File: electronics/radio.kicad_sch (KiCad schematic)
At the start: 26 parts, among them J7 SIM_Card, J9 Conn_Coaxial_Small, U2 TPS22953

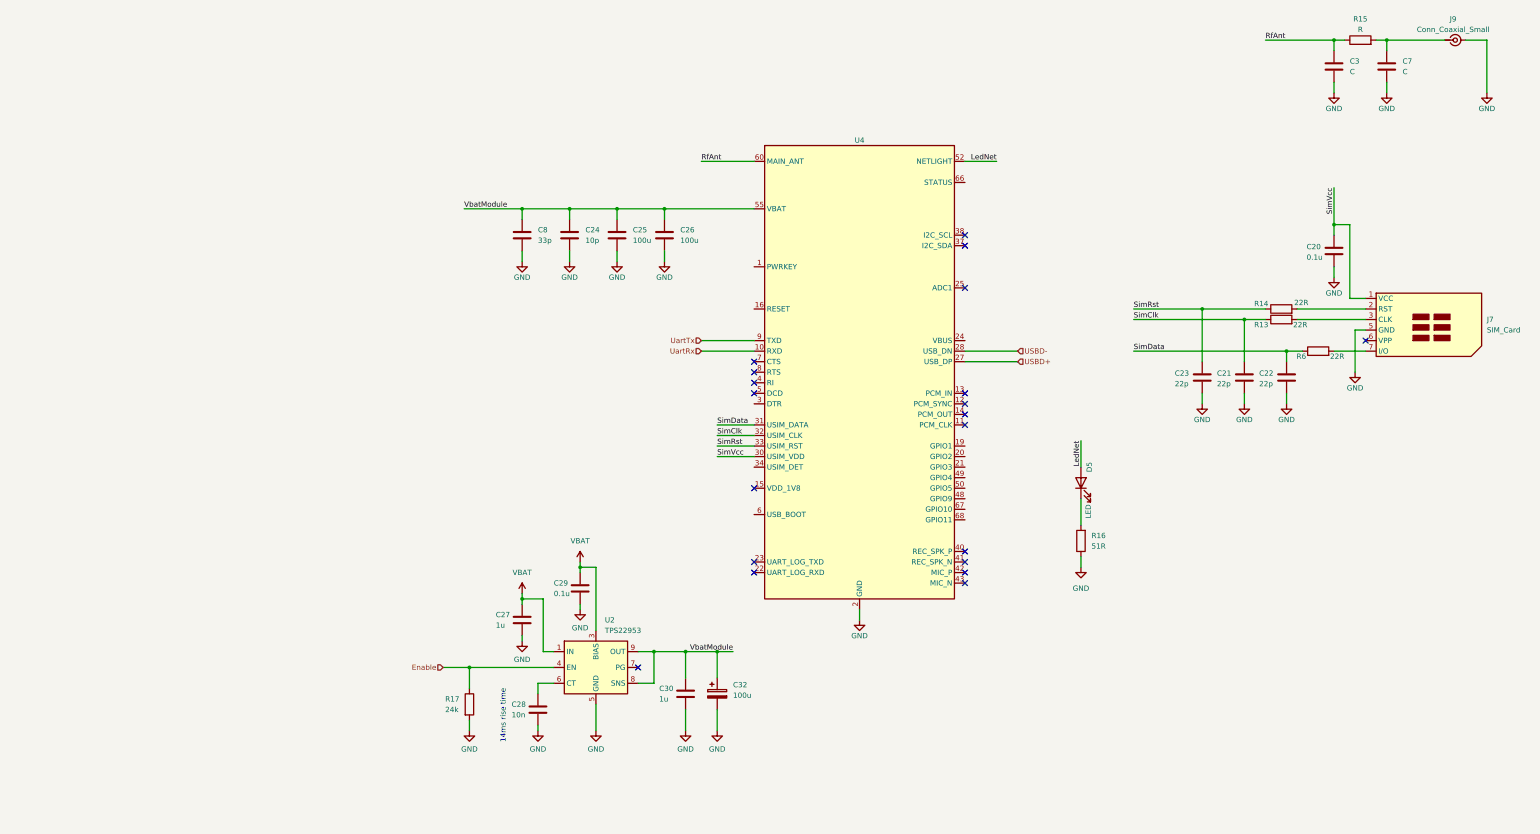
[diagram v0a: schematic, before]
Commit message: electronics: replace charger
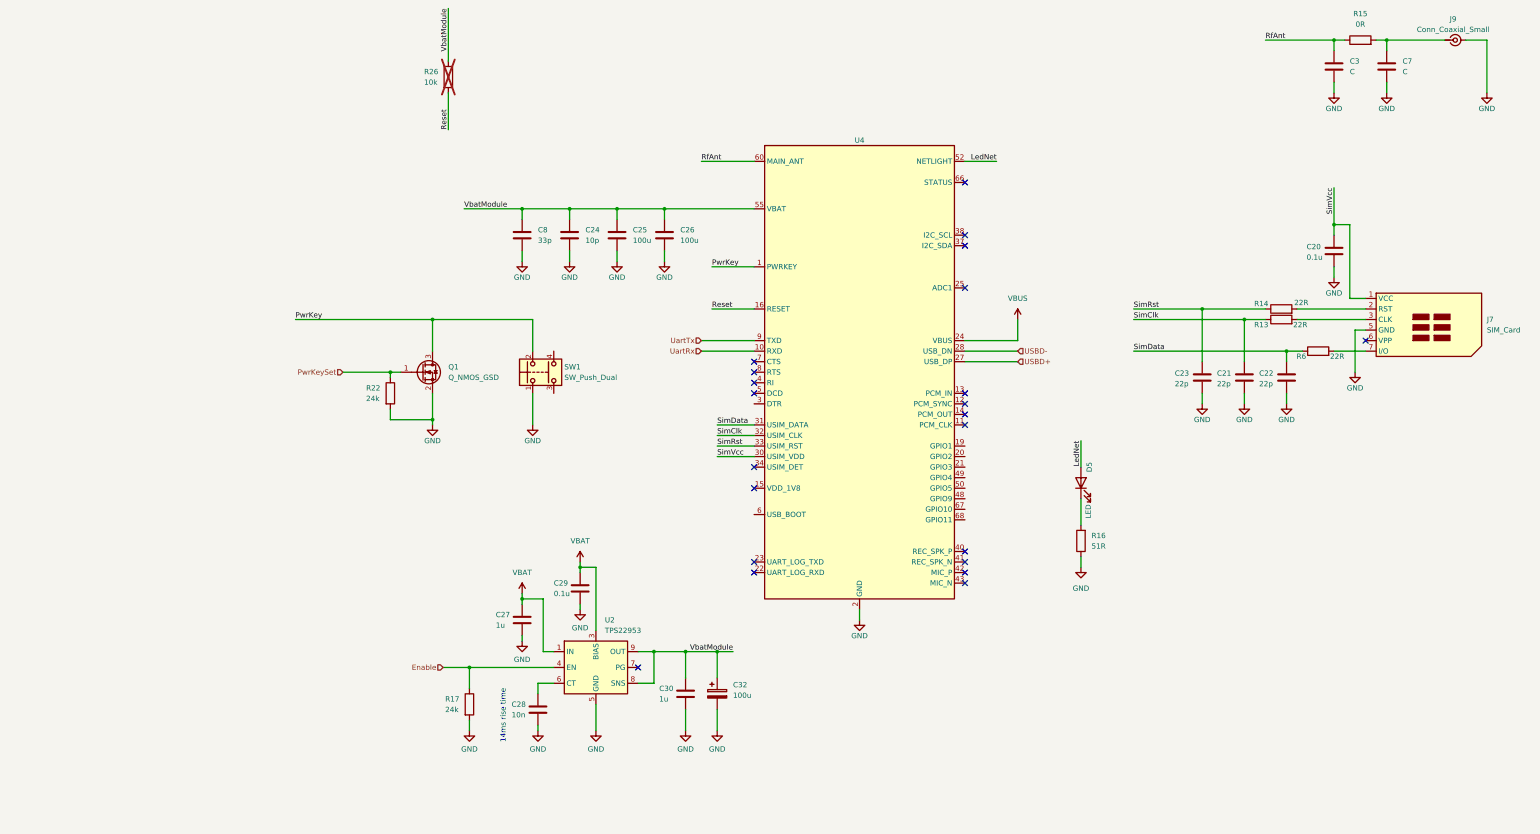
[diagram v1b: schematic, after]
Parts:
- added Q1: Q_NMOS_GSD, symbol Transistor_FET:Q_NMOS_GSD
- added R22: 24k, Resistor_SMD:R_0402_1005Metric, symbol Device:R
- added R26: 10k, Resistor_SMD:R_0402_1005Metric, symbol Device:R
- added SW1: SW_Push_Dual, symbol Switch:SW_Push_Dual
- C20, C21, C22, C23, C24, C8: footprint (none) -> Capacitor_SMD:C_0603_1608Metric
- C25, C26: footprint (none) -> Capacitor_SMD:C_1210_3225Metric
- C3, C7: footprint (none) -> Capacitor_SMD:C_0402_1005Metric
- C32: footprint portsupply:CP_Elec_6.3x7.7 -> Capacitor_SMD:CP_Elec_6.3x7.7
- J7: footprint (none) -> Connector_Card:nanoSIM_Hinged_CUI_NSIM-2-C
- R13, R14, R6: footprint (none) -> Resistor_SMD:R_0603_1608Metric
- R15: value R -> 0R; footprint (none) -> Resistor_SMD:R_0402_1005Metric
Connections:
- net GND: now also Q1.2 (S), R22.2, SW1.1
- net VBAT: now also R26.1
- net PwrKey: now reaches U4.1 (PWRKEY)
- net PwrKey: now also Q1.3 (D), SW1.2
- net Reset: now reaches U4.16 (RESET)
- net Reset: now also R26.2
- net VBUS: now reaches U4.24 (VBUS)
- new net PwrKeySet: Q1.1 (G), R22.1
- no-connect marks 20 -> 22

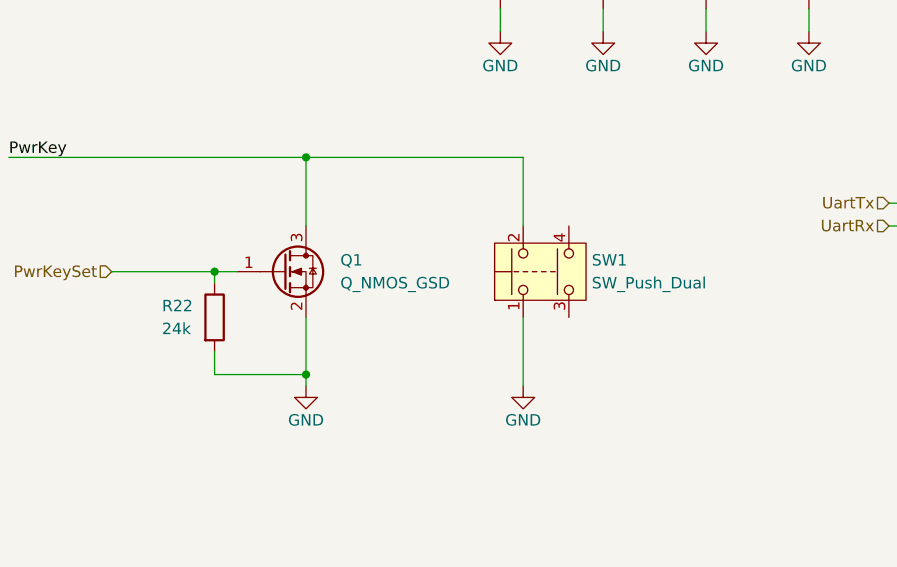
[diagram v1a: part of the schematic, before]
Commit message: electronics: select footprints
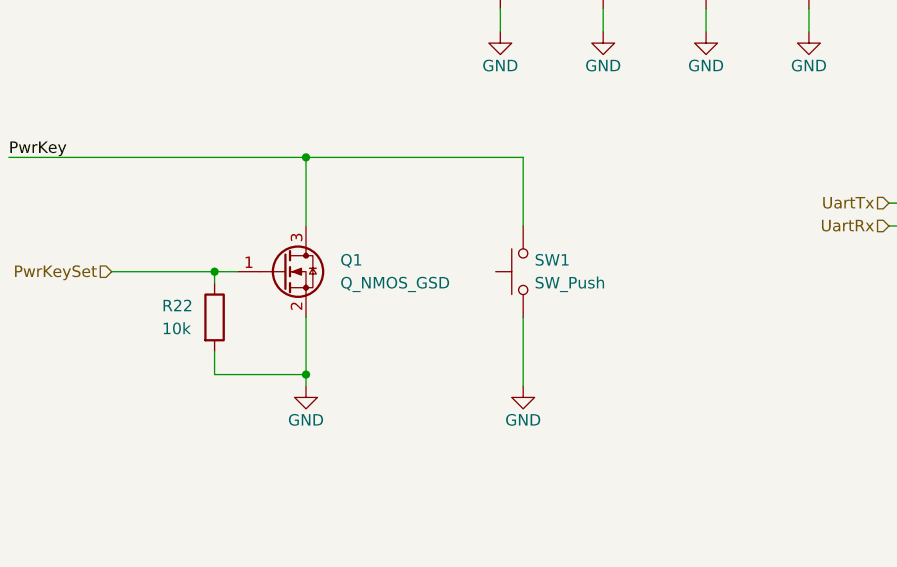
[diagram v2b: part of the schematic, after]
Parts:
- removed SW1: SW_Push_Dual, symbol Switch:SW_Push_Dual
- added SW1: SW_Push, Button_Switch_SMD:SW_SPST_TL3305A, symbol Switch:SW_Push
- J9: footprint (none) -> Connector_Coaxial:U.FL_Hirose_U.FL-R-SMT-1_Vertical; MPN (none) -> U.FL-R-SMT-1(01)
- R22: value 24k -> 10k
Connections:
- net GND: now also SW1.1
- net PwrKey: now also SW1.2
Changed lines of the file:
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@@
 	)
 	(symbol
-		(lib_id "Switch:SW_Push_Dual")
-		(at 48.26 101.6 90)
-		(unit 1)
-		(body_style 1)
-		(exclude_from_sim no)
-		(in_bom yes)
-		(on_board yes)
-		(in_pos_files yes)
-		(dnp no)
-		(fields_autoplaced yes)
-		(property "Reference" "SW1"
-			(at 53.34 100.3299 90)
-			(show_name no)
-			(do_not_autoplace no)
-			(effects
-				(font
-					(size 1.27 1.27)
-				)
-				(justify right)
-			)
-		)
-		(property "Value" "SW_Push_Dual"
-			(at 53.34 102.8699 90)
-			(show_name no)
-			(do_not_autoplace no)
-			(effects
-				(font
-					(size 1.27 1.27)
-				)
-				(justify right)
-			)
-		)
-		(property "Footprint" ""
-			(at 40.64 101.6 0)
-			(hide yes)
-			(show_name no)
-			(do_not_autoplace no)
-			(effects
-				(font
-					(size 1.27 1.27)
-				)
-			)
-		)
-		(property "Datasheet" ""
-			(at 48.26 101.6 0)
-			(hide yes)
-			(show_name no)
-			(do_not_autoplace no)
-			(effects
-				(font
-					(size 1.27 1.27)
-				)
-			)
-		)
-		(property "Description" "Push button switch, generic, symbol, four pins"
-			(at 48.26 101.6 0)
-			(hide yes)
-			(show_name no)
-			(do_not_autoplace no)
-			(effects
-				(font
-					(size 1.27 1.27)
-				)
-			)
-		)
-		(pin "1"
-		)
-		(pin "2"
-		)
-		(pin "4"
-		)
-		(pin "3"
-		)
-		(instances
-			(project "MyScale"
-				(path "/b5eed584-7820-40e8-871b-2aa5dd8c83ec/d79f2b7f-8f6c-4118-9551-ed509f2ef890"
-					(reference "SW1")
-					(unit 1)
-				)
-			)
-		)
-	)
-	(symbol
 		(lib_id "power:GND")
 		(at 43.18 166.37 0)
@@
 			)
 		)
-		(property "Value" "24k"
+		(property "Value" "10k"
 			(at 5.588 107.95 0)
 			(show_name no)
@@
 	)
 	(symbol
+		(lib_id "Switch:SW_Push")
+		(at 45.72 101.6 90)
+		(unit 1)
+		(body_style 1)
+		(exclude_from_sim no)
+		(in_bom yes)
+		(on_board yes)
+		(in_pos_files yes)
+		(dnp no)
+		(fields_autoplaced yes)
+		(property "Reference" "SW1"
+			(at 46.99 100.3299 90)
+			(show_name no)
+			(do_not_autoplace no)
+			(effects
+				(font
+					(size 1.27 1.27)
+				)
+				(justify right)
+			)
+		)
+		(property "Value" "SW_Push"
+			(at 46.99 102.8699 90)
+			(show_name no)
+			(do_not_autoplace no)
+			(effects
+				(font
+					(size 1.27 1.27)
+				)
+				(justify right)
+			)
+		)
+		(property "Footprint" "Button_Switch_SMD:SW_SPST_TL3305A"
+			(at 40.64 101.6 0)
+			(hide yes)
+			(show_name no)
+			(do_not_autoplace no)
+			(effects
+				(font
+					(size 1.27 1.27)
+				)
+			)
+		)
+		(property "Datasheet" ""
+			(at 40.64 101.6 0)
+			(hide yes)
+			(show_name no)
+			(do_not_autoplace no)
+			(effects
+				(font
+					(size 1.27 1.27)
+				)
+			)
+		)
+		(property "Description" "Push button switch, generic, two pins"
+			(at 45.72 101.6 0)
+			(hide yes)
+			(show_name no)
+			(do_not_autoplace no)
+			(effects
+				(font
+					(size 1.27 1.27)
+				)
+			)
+		)
+		(pin "1"
+		)
+		(pin "2"
+		)
+		(instances
+			(project "MyScale"
+				(path "/b5eed584-7820-40e8-871b-2aa5dd8c83ec/d79f2b7f-8f6c-4118-9551-ed509f2ef890"
+					(reference "SW1")
+					(unit 1)
+				)
+			)
+		)
+	)
+	(symbol
 		(lib_id "Device:R")
 		(at 226.06 88.9 90)
@@
 			)
 		)
-		(property "Footprint" ""
+		(property "Footprint" "Connector_Coaxial:U.FL_Hirose_U.FL-R-SMT-1_Vertical"
 			(at 267.97 21.59 0)
 			(hide yes)
@@
 			(at 267.97 21.59 0)
 			(hide yes)
+			(show_name no)
+			(do_not_autoplace no)
+			(effects
+				(font
+					(size 1.27 1.27)
+				)
+			)
+		)
+		(property "MPN" "U.FL-R-SMT-1(01)"
+			(at 267.97 21.59 0)
+			(hide yes)

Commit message: electronics: initial placement
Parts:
- Q1: footprint (none) -> Package_TO_SOT_SMD:SOT-23-3
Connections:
- net VBAT: no longer C24.1, C25.1, C26.1, C30.1, C32.1, C8.1, R26.1, U2.10 (OUT), U2.8 (SNS), U2.9 (OUT), U4.55 (VBAT), U4.56 (VBAT), U4.57 (VBAT)
- new net VbatModule: C24.1, C25.1, C26.1, C30.1, C32.1, C8.1, R26.1, U2.10 (OUT), U2.8 (SNS), U2.9 (OUT), U4.55 (VBAT), U4.56 (VBAT), U4.57 (VBAT)
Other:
- moved on the sheet: C30, C32

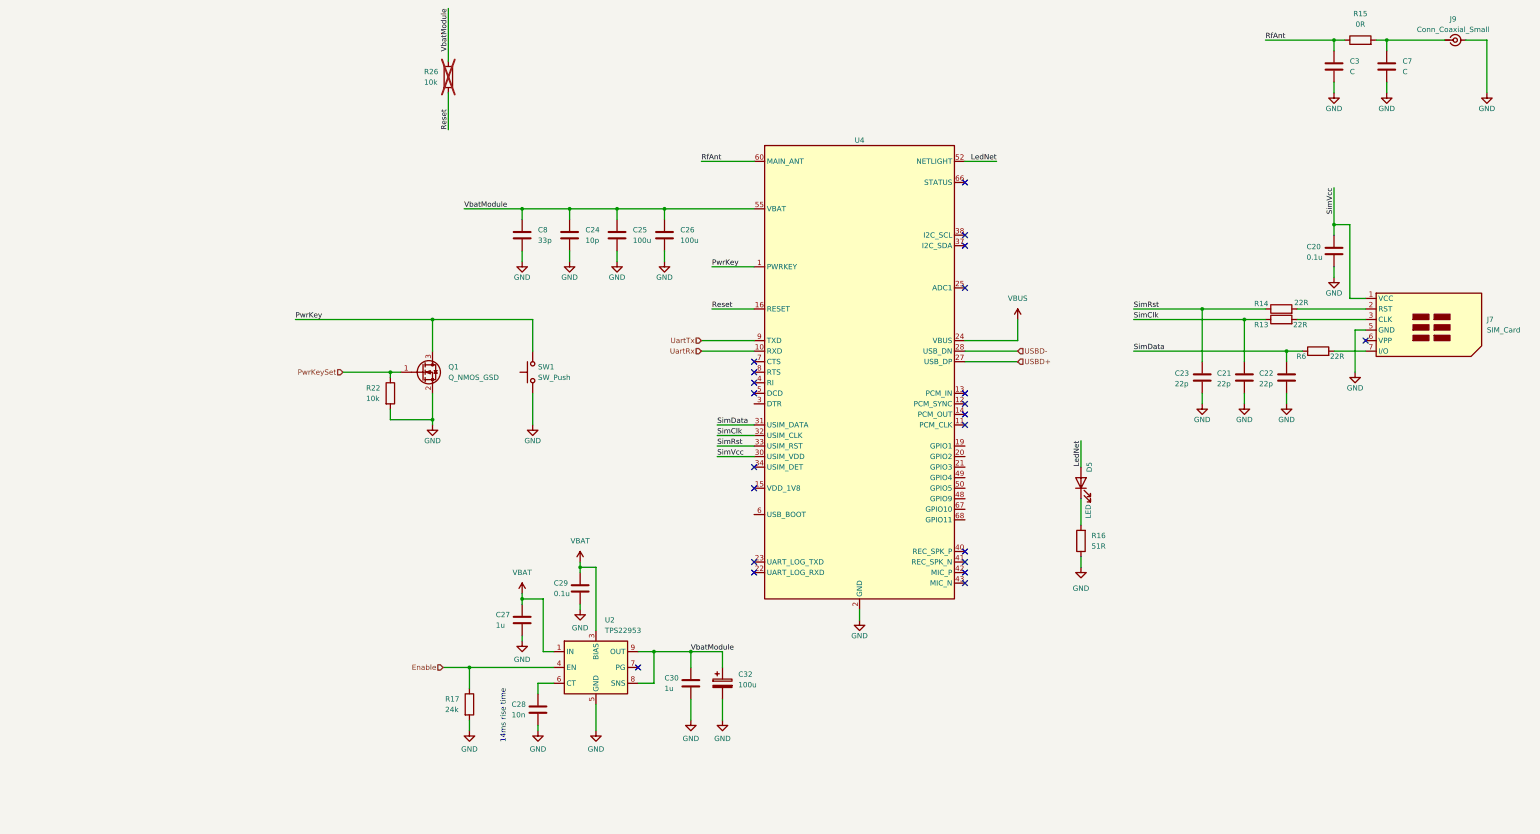
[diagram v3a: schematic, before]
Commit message: electronics: replace A7670 footprint
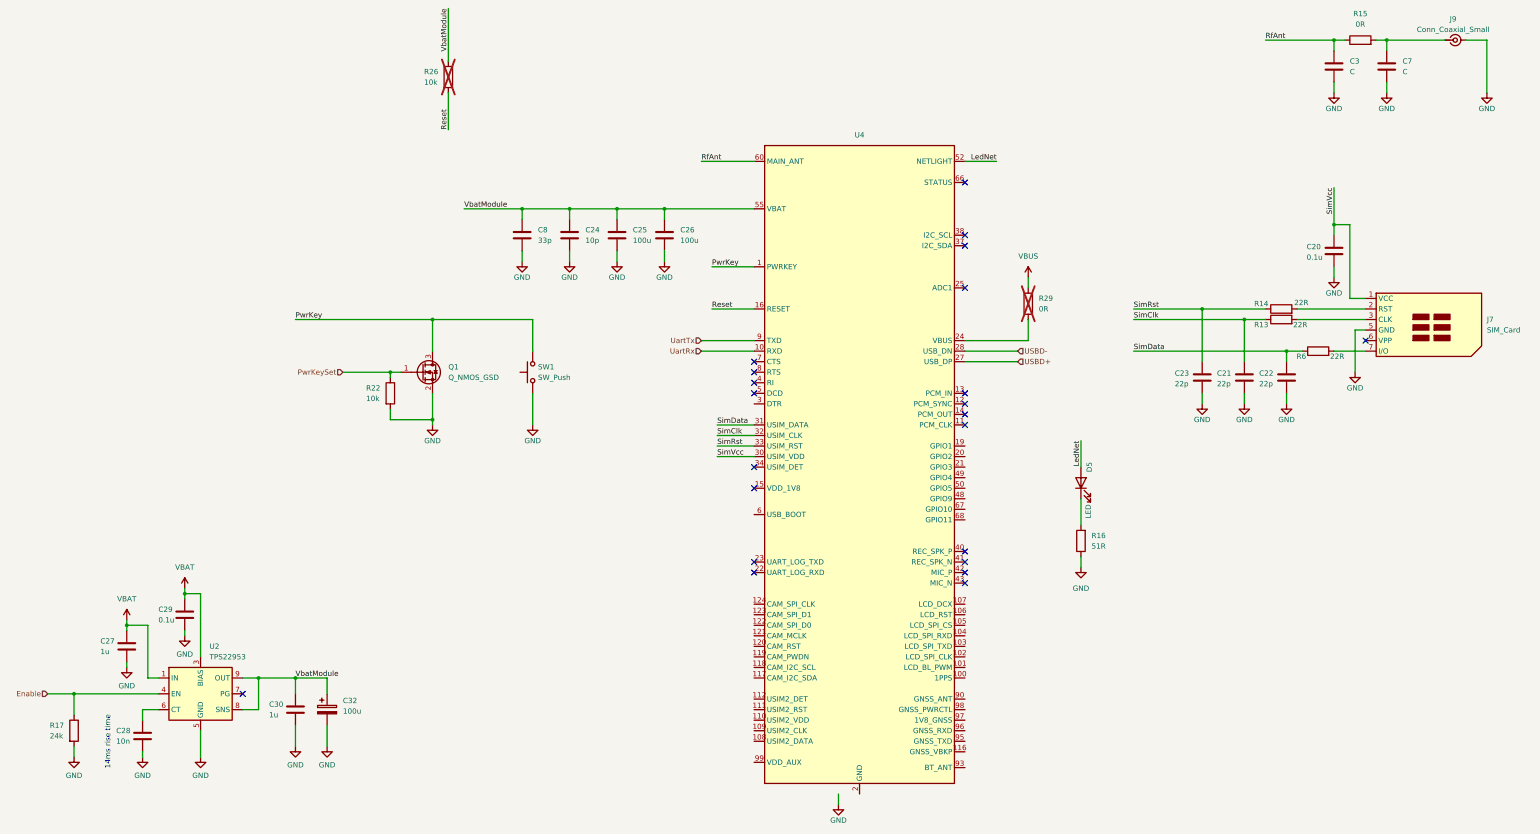
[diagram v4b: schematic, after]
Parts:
- added R29: 0R, Resistor_SMD:R_0603_1608Metric, symbol Device:R
- U4: footprint MyScale:A7670 -> MyScale:A7670_STAMP; symbol MyScale:A7670 -> MyScale:A7670_STAMP
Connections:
- net GND: now also U4.89 (GND), U4.91 (GND), U4.92 (GND), U4.94 (GND)
- net VBUS: now also R29.2; no longer U4.24 (VBUS)
- new net: R29.1, U4.24 (VBUS)
- now unconnected: U4.26 (NC), U4.35 (NC), U4.36 (NC), U4.44 (NC), U4.47 (NC), U4.51 (NC), U4.53 (NC)
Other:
- moved on the sheet: C27, C28, C29, C30, C32, R17, U2

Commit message: electronics: add 3D models
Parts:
- added TP1: TestPoint, symbol Connector:TestPoint
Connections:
- net GND: now also U4.98 (GNSS_PWRCTL)
- net at U4.6 (USB_BOOT): now also TP1.1
- no-connect marks 22 -> 49

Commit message: electronics: final touches
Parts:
- removed R15: 0R, Resistor_SMD:R_0402_1005Metric, symbol Device:R
- added R31: 0R, Resistor_SMD:R_0603_1608Metric, symbol Device:R
- added TP2: TestPoint, TestPoint:TestPoint_Pad_D1.0mm, symbol Connector:TestPoint
- C3, C7: now not fitted; now left out of the parts list
- J7: symbol Connector:SIM_Card -> MyScale:SIM_Card_Shielded_Det
- TP1: footprint (none) -> TestPoint:TestPoint_Pad_D1.0mm
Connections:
- net GND: now also J7.SH
- net RfAnt: now also C7.1, J9.1 (In)
- net at U4.23 (UART_LOG_TXD): now also TP2.1
- net at U4.34 (USIM_DET): now also R31.1
- new net SimDet: J7.CD, R31.2
- no-connect marks 49 -> 57
